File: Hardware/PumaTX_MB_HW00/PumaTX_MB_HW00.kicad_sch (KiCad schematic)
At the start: 57 parts, among them J100 FH12A-26S-0.5SH_55_, J101 FH12-12S-0.5SH_55_, J102 500334-0160, J103 500334-0160, J104 692122030100, J105 53398-0667, J106 Conn_01x02_Male, J107 Conn_01x02_Male, J410 U.FL-R-SMT-1_40_, Q200 UMH3NTN, Q201 UMH3NTN, U200 CP2105-F01-GMR, U300 ESP32-PICO-D4, U400 ESP32-PICO-D4, U402 E28-2G4M27S, U410 SX1280, U500 BQ24075RGTR, U510 MIC5528-3.3YMT-T5, U520 MIC5528-3.3YMT-T5, U530 MIC5528-3.3YMT-T5

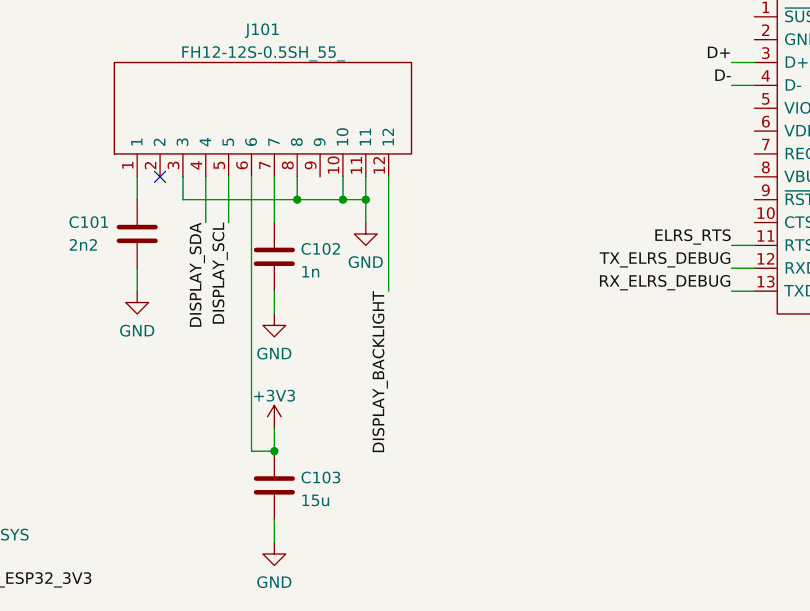
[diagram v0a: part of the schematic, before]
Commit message: Added display consumption
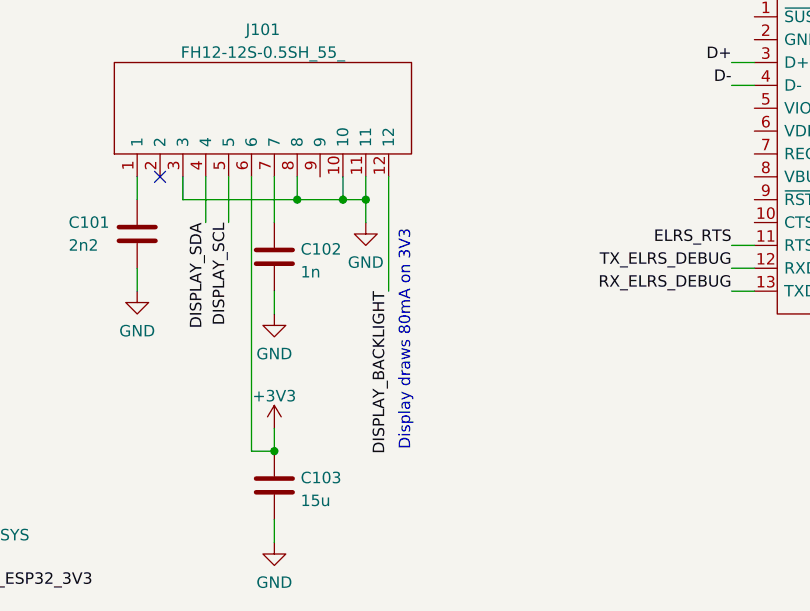
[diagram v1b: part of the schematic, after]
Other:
- note added: "Display draws 80mA on 3V3"
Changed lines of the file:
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@@
+    (effects (font (size 1.27 1.27)) (justify left bottom))
+  )
+  (text "Display draws 80mA on 3V3" (at 203.2 81.28 90)
     (effects (font (size 1.27 1.27)) (justify left bottom))
   )

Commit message: Minor updates
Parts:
- added J?: U.FL-R-SMT-1_40_, Component_lib:u.fl, symbol Component lib:U.FL-R-SMT-1_40_
- added Q100: UMH3NTN, Component_lib:UMH3NTN, symbol Component_lib:UMH3NTN
- BZ100: footprint Component_lib:GL200A_BUZZER -> (none)
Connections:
- net +3V3: no longer R300.1, R401.1
- net BUZZER_PWM: now also BZ100.1 (-)
- net ELRS_ESP32_3V3: now also R401.1
- net FAN_PWM: now also Q100.5 (B2)
- net GND: now also BZ100.2 (+)
- net HAPTIC_PWM: now also Q100.2 (B1)
- net PUMATX_ESP32_3V3: now also R300.1
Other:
- moved on the sheet: C300, J106, J107, R300, TP300

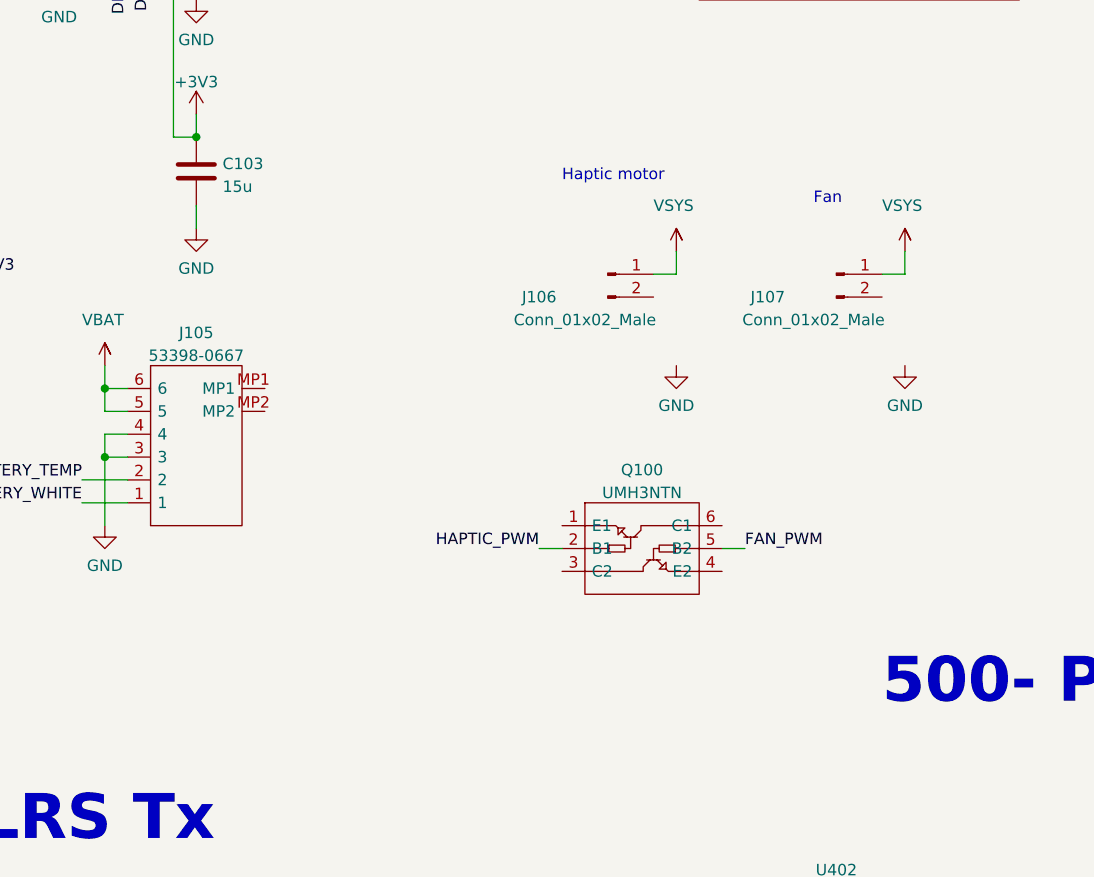
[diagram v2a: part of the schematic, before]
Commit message: Changed motor and fan schematics
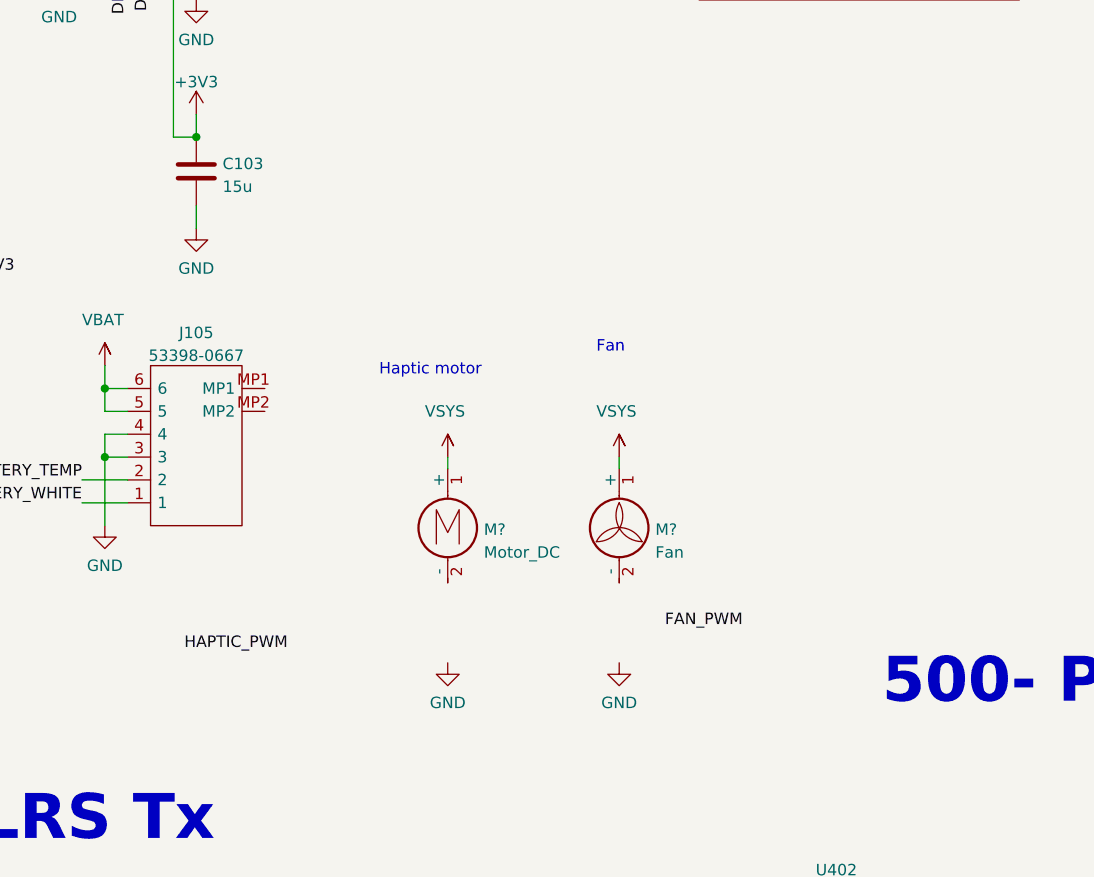
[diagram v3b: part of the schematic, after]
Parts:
- removed J106: Conn_01x02_Male, Component_lib:GL200A_HAPTIC_MOTOR, symbol Connector:Conn_01x02_Male
- removed J107: Conn_01x02_Male, Connector_PinHeader_1.27mm:PinHeader_1x02_P1.27mm_Horizontal, symbol Connector:Conn_01x02_Male
- removed Q100: UMH3NTN, Component_lib:UMH3NTN, symbol Component_lib:UMH3NTN
- added M?: Fan, symbol Component lib:Fan
- added M?: Motor_DC, symbol Component lib:Motor_DC

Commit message: Finished BQ, EPS32 integration
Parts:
- removed J?: U.FL-R-SMT-1_40_, Component_lib:u.fl, symbol Component lib:U.FL-R-SMT-1_40_
- added ANT400: 2450AT18A100E, ANTC3216X140N, symbol Component_lib:2450AT18A100E
- added C306, C307, C406, C407: C, symbol Component_lib:C
- added C350, C450: 100n, Capacitor_SMD:C_0402_1005Metric, symbol Component_lib:C
- added C351, C451: 1u, Capacitor_SMD:C_0402_1005Metric, symbol Component_lib:C
- added C352, C452: 10u, Capacitor_SMD:C_0402_1005Metric, symbol Component_lib:C
- added D500, D501: LED, symbol Component_lib:LED
- added J300: U.FL-R-SMT-1_40_, UFLRSMT140, symbol Component_lib:U.FL-R-SMT-1_40_
- added L300, L400: L, symbol Component_lib:L
- added Q130, Q140: ZXMN3B01F, Package_TO_SOT_SMD:SOT-23, symbol Component_lib:ZXMN3B01F
- added R130, R140: 180, symbol Component_lib:R
- added R131, R141: 10k, symbol Component_lib:R
- added R501: 100k, symbol Component_lib:R
- added R502: 1k1, symbol Component_lib:R
- added R503: 590, symbol Component_lib:R
- added R504: 0, symbol Component_lib:R
- added R505: 36k5, symbol Component_lib:R
- added R506, R507: 1k5, symbol Component_lib:R
- added R510: 0k, symbol Component_lib:R
- added TP301, TP401: VDD_SDIO, TestPoint:TestPoint_Pad_D1.5mm, symbol Connector:TestPoint
- TP300: value TestPoint -> PUMATX_PU
- gave numbers to parts that had none: 2
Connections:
- net +3V3: no longer R301.1, R302.1, R303.1, R304.1
- net ELRS_ESP32_3V3: now also U400.1 (VDDA), U400.19 (VDD3P3_RTC), U400.3 (VDD3P3), U400.37 (VDD3P3_CPU), U400.4 (VDD3P3), U400.43 (VDDA), U400.46 (VDDA), C450.1, C451.1, C452.1
- net FAN_PWM: now also R140.2, R141.1
- net GND: now also U500.6 (EN1), C306.2, C307.2, C350.2, C351.2, C352.2, C406.2, C407.2, C450.2, C451.2, C452.2, J300.2 (gnd), J300.3 (gnd), Q130.2 (S), Q140.2 (S), R131.2, R141.2, R501.2, R502.1, R503.2, R504.2, R505.2
- net HAPTIC_PWM: now also R130.2, R131.1
- net LED: now also U520.4 (EN), U530.4 (EN)
- net PUMATX_ESP32_3V3: now also R301.1, R302.1, R303.1, R304.1, U300.1 (VDDA), U300.19 (VDD3P3_RTC), U300.3 (VDD3P3), U300.37 (VDD3P3_CPU), U300.4 (VDD3P3), U300.43 (VDDA), U300.46 (VDDA), C350.1, C351.1, C352.1
- net V_PA: now reaches C410.1, U410.1 (VR_PA)
- net at C510.1, U510.6 (VIN): now also R510.2
- net at U300.2 (LNA_IN): now also C306.1, L300.2
- net at U300.26 (VDD_SDIO): now also TP301.1
- net at U400.2 (LNA_IN): now also C406.1, L400.2
- net at U400.26 (VDD_SDIO): now also TP401.1
- net at U510.4 (EN): now also R510.1
- net at U500.12 (ILIM): now also R502.2
- net at U500.14 (TMR): now also R505.1
- net at U500.15 (SYSOFF): now also R504.1
- net at U500.16 (ISET): now also R503.1
- net at U500.4 (~{CE}): now also R501.1
- net BQ_PGOOD: now reaches U500.7 (~{PGOOD})
- net BQ_PGOOD: now also D500.1 (K)
- net BQ_CHG: now reaches U500.9 (~{CHG})
- net BQ_CHG: now also D501.1 (K)
- net at M140.2 (-): now also Q140.3 (D)
- net at M130.2 (-): now also Q130.3 (D)
- new net: Q140.1 (G), R140.1
- new net: D500.2 (A), R506.2
- new net: D501.2 (A), R507.2
- new net: C307.1, J300.1 (ant), L300.1
- new net: R506.1, R507.1
- new net: ANT400.1 (A), C407.1, L400.1
- new net: Q130.1 (G), R130.1
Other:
- note added: "1550/Iin=R502"
- note added: "1u to 10u"
- note added: "36k5: 5h safety 30min pre charge"
- note added: "4u7 to 47u"
- note added: "890/Ichg=R503"
- note added: "SYSOFF low for normal operation"
- moved on the sheet: C300, C302, C303, C304, C501, C502, C503, C510, C520, C530, M130, M140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

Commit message: Almost done!
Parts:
- added C200, C202: 1u, Capacitor_SMD:C_0603_1608Metric, symbol Component lib:C
- added C201, C203: 100n, Capacitor_SMD:C_0603_1608Metric, symbol Component lib:C
- added C410: 0p8, Capacitor_SMD:C_0603_1608Metric, symbol Component_lib:C
- added C411, C412: 1p2, Capacitor_SMD:C_0603_1608Metric, symbol Component_lib:C
- added C413: 100p, Capacitor_SMD:C_0603_1608Metric, symbol Component_lib:C
- added C414: 0p5, Capacitor_SMD:C_0603_1608Metric, symbol Component_lib:C
- added C418: 100n, Capacitor_SMD:C_0603_1608Metric, symbol Component_lib:C
- added D130, D140: S1GHE, Component_lib:S1GHE, symbol Component lib:S1GHE
- added L411: 3n, Capacitor_SMD:C_0402_1005Metric, symbol Component lib:L
- added L412: 2n5, Capacitor_SMD:C_0402_1005Metric, symbol Component lib:L
- added L414: 15u, Capacitor_SMD:C_0805_2012Metric, symbol Component lib:L
- added R200: 4k7, symbol Component lib:R
- added Y410: NX2016SA-52MHZ-EXS00A-CS06016, Component_lib:NX2016SA32MEXS00ACS06465, symbol Component lib:NX2016SA-52MHZ-EXS00A-CS06016
- ANT400: footprint ANTC3216X140N -> Component_lib:ANTC3216X140N
- BZ100: footprint (none) -> Component_lib:GL200A_BUZZER
- C306, C307, C406, C407, D500, D501, L300, L400, R130, R131, R140, R141, R501, R502, R503, R504, R505, R506, R507, R510: footprint (none) -> Capacitor_SMD:C_0402_1005Metric
- J300: footprint UFLRSMT140 -> Component_lib:u.fl
- M130: footprint (none) -> Component_lib:GL200A_HAPTIC_MOTOR
- M140: footprint (none) -> Component_lib:SM02B-SURS-TF
- U510, U520, U530: footprint SON40P120X120X60-7N-D -> Component_lib:SON40P120X120X60-7N-D
- renumbered C410 to C415, C411 to C416, C413 to C419, C412 to C420
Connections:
- net 3V3_ELRS is gone; now on net SX1280_3V3: C420.1, U410.11 (VBAT_IO), U410.15 (VBAT)
- net GND: now also U200.2 (GND), U200.25 (EP), C200.2, C201.2, C202.2, C203.2, C410.2, C411.2, C412.2, C418.2, Y410.2
- net PUMATX_ESP32_3V3: now also U200.5 (VIO), C203.1, R200.2
- net SX1280_3V3: now also C418.1
- net VBUS: now also U200.7 (REGIN), U200.8 (VBUS), C200.1
- net V_DCC2: now reaches U410.14 (DCC_SW)
- net V_DCC2: now also L414.2
- net at U410.22 (RFIO): now also C410.1, L411.1; no longer J410.1 (ant)
- net XTA: now reaches U410.4 (XTA)
- net XTA: now also Y410.3
- net XTB: now reaches U410.6 (XTB)
- net XTB: now also Y410.1
- net at M140.2 (-), Q140.3 (D): now also D140.2 (A)
- net 3V45: now reaches U200.6 (VDD)
- net 3V45: now also C201.1, C202.1
- net at U200.9 (~{RST}): now also R200.1
- net at M140.1 (+): now also D140.1 (K)
- net at M130.2 (-), Q130.3 (D): now also D130.2 (A)
- net at M130.1 (+): now also D130.1 (K)
- net IRS renamed V_DCC
- net V_DCC: now also L414.1
- new net: C411.1, C414.1, L411.2, L412.1
- new net: C412.1, C413.1, C414.2, L412.2
- new net: C413.2, J410.1 (ant)
- no-connect marks 26 -> 25
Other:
- note added: "close to regin"
- note added: "close to vio"
- moved on the sheet: C419, C420, C501, C502, C503, Q200, Q201, U200

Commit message: Schematic is "done"
Functionaly it is done, but could get some cleanup
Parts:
- added D200: SP0503BAHTG, Component_lib:SP0503BAHTG, symbol Component lib:SP0503BAHTG
- R130, R140: value 180 -> 10k
- R131, R141: value 10k -> 180
- R200: footprint (none) -> Capacitor_SMD:C_0402_1005Metric
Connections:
- net PUMATX_ESP32_3V3 is gone; now on net +3V3: C110.1, C120.1, C203.1, C350.1, C351.1, C352.1, C511.1, J104.3 (D+), R110.1, R120.1, R200.2, R300.1, R301.1, R302.1, R303.1, R304.1, U200.5 (VIO), U300.1 (VDDA), U300.19 (VDD3P3_RTC), U300.3 (VDD3P3), U300.37 (VDD3P3_CPU), U300.4 (VDD3P3), U300.43 (VDDA), U300.46 (VDDA), U510.1 (VOUT_1), U510.2 (VOUT_2)
- net CRSF: now also J104.7 (DRAIN); no longer J104.6 (SSRX+)
- net D+: now also D200.3 (K)
- net D-: now also D200.4 (K)
- net FAN_PWM: now also R140.1, R141.2; no longer R140.2, R141.1
- net GND: now also J100.MP1, J100.MP2, J105.MP1, J105.MP2, R130.2, R140.2, D200.1 (A); no longer R131.2, R141.2
- net HAPTIC_PWM: now also R130.1, R131.2; no longer R130.2, R131.1
- net RX_PUMATX_DEBUG: now also J104.6 (SSRX+)
- net TX_PUMATX_DEBUG: now also J104.5 (SSRX-)
- net VBUS: now also D200.2 (K)
- net 50_ELRS_ANT_2: now reaches C411.1, C414.1, L411.2, L412.1
- net 50_ELRS_ANT_1: now reaches C410.1, L411.1, U410.22 (RFIO)
- net TMR: now reaches R505.1, U500.14 (TMR)
- net 50_ELRS_ANT_3: now reaches C412.1, C413.1, C414.2, L412.2
- net 50_ELRS_ANT_4: now reaches C413.2, J410.1 (ant)
- net VDD_SDIO_ELRS: now reaches TP401.1, U400.26 (VDD_SDIO)
- net FAN_G: now reaches Q140.1 (G)
- net FAN_G: now also R141.1; no longer R140.1
- net FAN_LS: now reaches D140.2 (A), M140.2 (-), Q140.3 (D)
- net RST: now reaches R200.1, U200.9 (~{RST})
- net LED_PG: now reaches D500.2 (A), R506.2
- net VDD_SDIO_PUMATX: now reaches TP301.1, U300.26 (VDD_SDIO)
- net LED_CHG: now reaches D501.2 (A), R507.2
- net 50_PUMATX_ANT_2: now reaches C307.1, J300.1 (ant), L300.1
- net SYSOFF: now reaches R504.1, U500.15 (SYSOFF)
- net VSYS: now reaches J104.2 (D-)
- net VSYS: now also C510.1, R510.2, U500.10 (OUT_1), U500.11 (OUT_2), U500.5 (EN2), U510.6 (VIN)
- net DISPLAY_DECOUPLE_2: now reaches C102.1, J101.7
- net DISPLAY_DECOUPLE_1: now reaches C101.1, J101.1
- net SYS: now reaches R506.1, R507.1
- net 50_ESP_ELRS_ANT_2: now reaches ANT400.1 (A), C407.1, L400.1
- net 50_ESP_ELRS_ANT_1: now reaches C406.1, L400.2, U400.2 (LNA_IN)
- net 50_PUMATX_ANT_1: now reaches C306.1, L300.2, U300.2 (LNA_IN)
- net FAN_HS: now reaches D140.1 (K), M140.1 (+)
- net HAPTIC_G: now reaches Q130.1 (G)
- net HAPTIC_G: now also R131.1; no longer R130.1
- net ILIM: now reaches R502.2, U500.12 (ILIM)
- net VBAT: now reaches J105.5, J105.6
- net VBAT: now also C503.1, U500.2 (BAT_1), U500.3 (BAT_2)
- net 3V3_EN: now reaches R510.1, U510.4 (EN)
- net BQ_CE: now reaches R501.1, U500.4 (~{CE})
- net ISET: now reaches R503.1, U500.16 (ISET)
- net HAPTIC_HS: now reaches D130.1 (K), M130.1 (+)
- net HAPTIC_LS: now reaches D130.2 (A), M130.2 (-), Q130.3 (D)
- net ELRS_ESP32_3V3 renamed -3V3
- no-connect marks 25 -> 43
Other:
- note added: "not really -3v3, just convinient"
- moved on the sheet: ANT400, BZ100, C101, C102, C103, C110, C120, C200, C201, C202, C203, C300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

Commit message: Generated BOM and changed 2 capa footprints
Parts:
- C350, C450: footprint Capacitor_SMD:C_0402_1005Metric -> Capacitor_SMD:C_0603_1608Metric
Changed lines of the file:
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@@
       (effects (font (size 1.27 1.27)) (justify left))
     )
-    (property "Footprint" "Capacitor_SMD:C_0402_1005Metric" (id 2) (at 82.2452 365.76 0)
+    (property "Footprint" "Capacitor_SMD:C_0603_1608Metric" (id 2) (at 82.2452 365.76 0)
       (effects (font (size 1.27 1.27)) hide)
     )
@@
       (effects (font (size 1.27 1.27)) (justify left))
     )
-    (property "Footprint" "Capacitor_SMD:C_0402_1005Metric" (id 2) (at 252.4252 309.88 0)
+    (property "Footprint" "Capacitor_SMD:C_0603_1608Metric" (id 2) (at 252.4252 309.88 0)
       (effects (font (size 1.27 1.27)) hide)
     )
@@
     )
     (path "/21165a41-465d-422c-a6c6-98e661168a36"
-      (reference "C350") (unit 1) (value "100n") (footprint "Capacitor_SMD:C_0402_1005Metric")
+      (reference "C350") (unit 1) (value "100n") (footprint "Capacitor_SMD:C_0603_1608Metric")
     )
     (path "/baaa99be-d98b-4ae1-98d2-b25c1faf1791"
@@
     )
     (path "/ac267b7d-699c-492f-952c-5333be753890"
-      (reference "C450") (unit 1) (value "100n") (footprint "Capacitor_SMD:C_0402_1005Metric")
+      (reference "C450") (unit 1) (value "100n") (footprint "Capacitor_SMD:C_0603_1608Metric")
     )
     (path "/d850612a-e17f-44ca-bf5e-25c8066428d5"
